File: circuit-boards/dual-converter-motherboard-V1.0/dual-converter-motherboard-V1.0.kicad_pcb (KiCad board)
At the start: 6 copper layers, 230 x 76 mm, 130 parts, among them J1 2601-1102, J2 2601-1102, J3 S4B-XH-SM4-TB, Q1 SUM110P08-11L-E3, Q2 DMP45H4D9HK3-13, Q3 SIHB068N60EF-GE3, U1 POWER_MANAGEMENT_MODULE, U2 HIGH-CURRENT_PHASE_MODULE_V1.0, U3 HIGH-VOLTAGE_PHASE_MODULE, U4 UCC23313BDWYR, U5 TMCS1133C1A, U6 UCC23313BDWYR, U7 UCC23313BDWYR, U8 SC0915

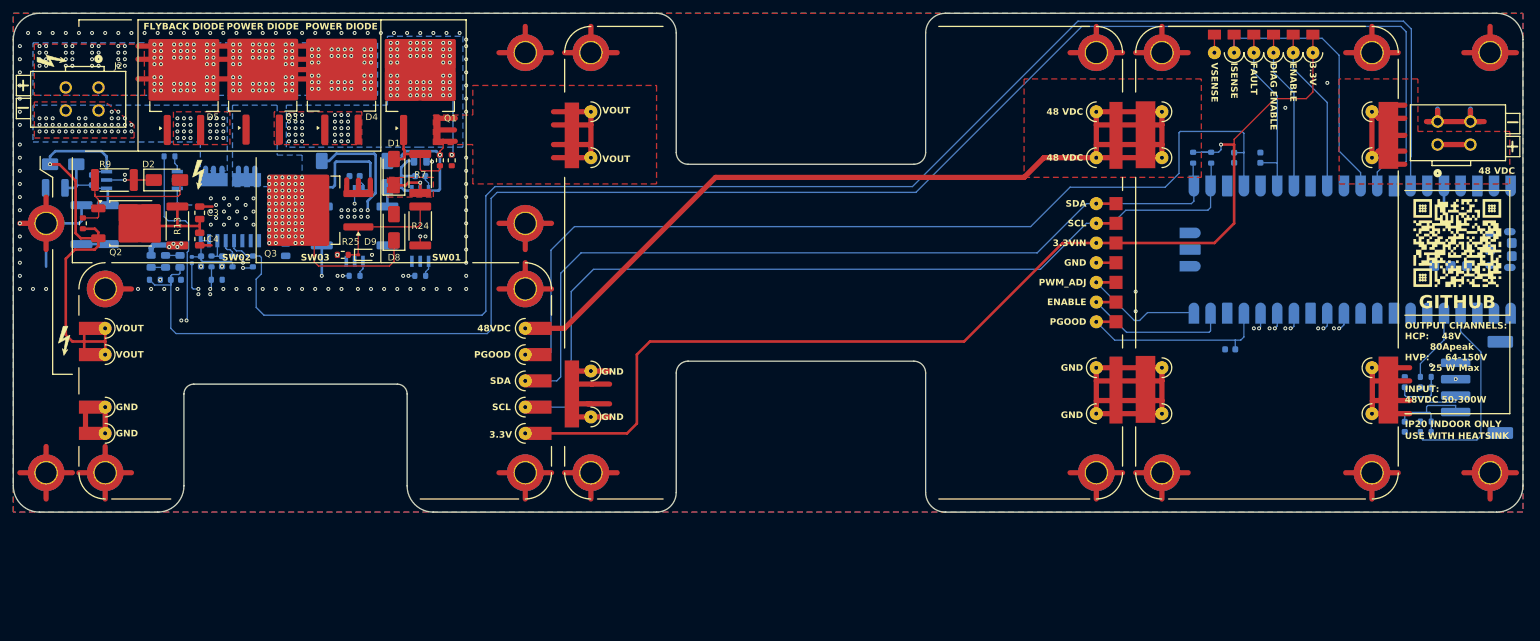
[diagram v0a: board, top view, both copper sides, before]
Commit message: begin replacing pogo pins with pin headers. todo: fix ugly schematic, add non power connections
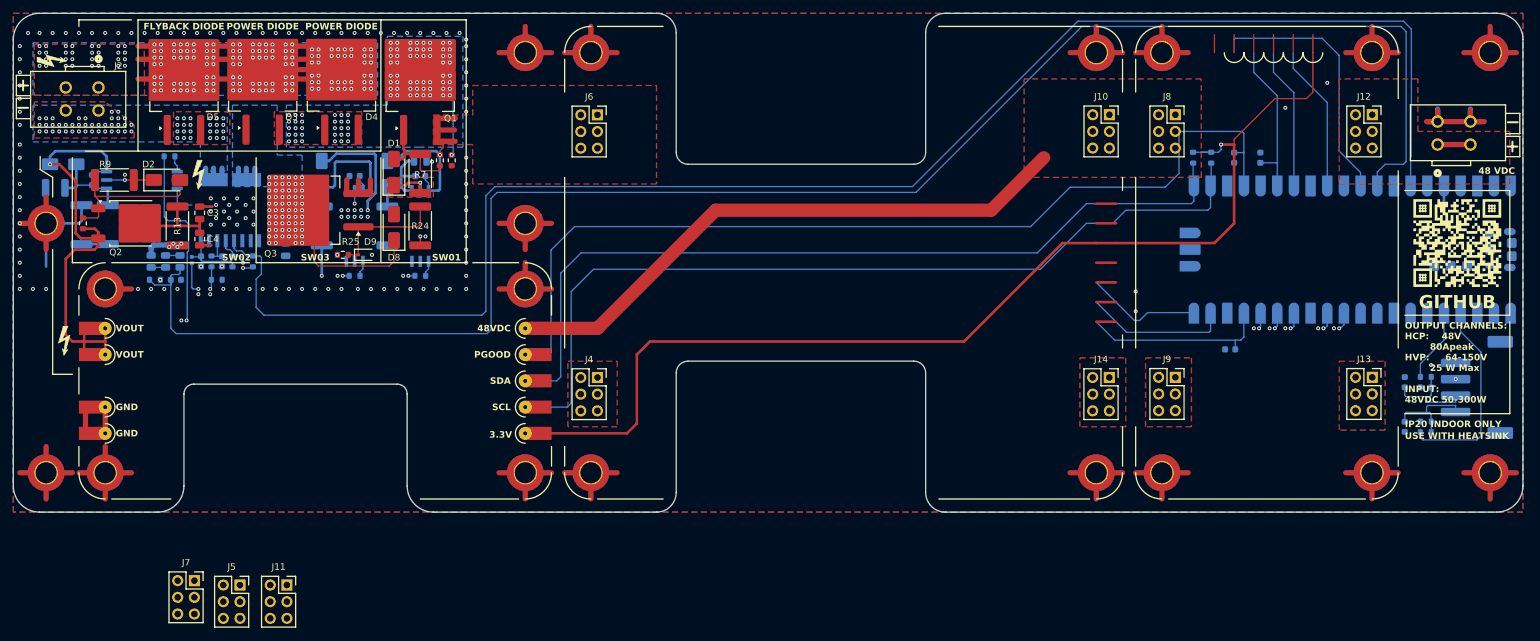
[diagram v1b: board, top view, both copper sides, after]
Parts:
- removed POGO10, POGO11, POGO12, POGO13, POGO14, POGO15, POGO16, POGO17, POGO18, POGO19, POGO20, POGO21, POGO27, POGO28, POGO29, POGO30: 0906-8-15-20-76-14-11-0, powercore-development:0906-8-15-20-76-14-11-0
- removed U1: POWER_MANAGEMENT_MODULE, powercore-development:POWER_MANAGEMENT_MODULE_FOOTPRINT_V1.0
- removed U2: HIGH-CURRENT_PHASE_MODULE_V1.0, powercore-development:HIGH-CURRENT_PHASE_MODULE_FOOTPRINT_V1.0
- added J10: Conn_02x03_Odd_Even, Connector_PinSocket_2.54mm:PinSocket_2x03_P2.54mm_Vertical, F.Cu at (189.0, 43.5)
- added J11: Conn_02x03_Odd_Even, Connector_PinSocket_2.54mm:PinSocket_2x03_P2.54mm_Vertical, F.Cu at (63.7, 115.1)
- added J12: Conn_02x03_Odd_Even, Connector_PinSocket_2.54mm:PinSocket_2x03_P2.54mm_Vertical, F.Cu at (229.0, 43.5)
- added J13: Conn_02x03_Odd_Even, Connector_PinSocket_2.54mm:PinSocket_2x03_P2.54mm_Vertical, F.Cu at (229.0, 83.5)
- added J14: Conn_02x03_Odd_Even, Connector_PinSocket_2.54mm:PinSocket_2x03_P2.54mm_Vertical, F.Cu at (189.0, 83.5)
- added J4: Conn_02x03_Odd_Even, Connector_PinSocket_2.54mm:PinSocket_2x03_P2.54mm_Vertical, F.Cu at (111.0, 83.5)
- added J5: Conn_02x03_Odd_Even, Connector_PinSocket_2.54mm:PinSocket_2x03_P2.54mm_Vertical, F.Cu at (56.5, 115.1)
- added J6: Conn_02x03_Odd_Even, Connector_PinSocket_2.54mm:PinSocket_2x03_P2.54mm_Vertical, F.Cu at (111.0, 43.5)
- added J7: Conn_02x03_Odd_Even, Connector_PinSocket_2.54mm:PinSocket_2x03_P2.54mm_Vertical, F.Cu at (49.6, 114.4)
- added J8: Conn_02x03_Odd_Even, Connector_PinSocket_2.54mm:PinSocket_2x03_P2.54mm_Vertical, F.Cu at (199.0, 43.5)
- added J9: Conn_02x03_Odd_Even, Connector_PinSocket_2.54mm:PinSocket_2x03_P2.54mm_Vertical, F.Cu at (199.0, 83.5)
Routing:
- net GND: track 418.5 -> 306.5 mm
- net +48V: track 195.1 -> 133.1 mm
- net /BUCK-CONVERTER-OUTPUT: track 57.5 -> 28.9 mm
- net /48VIN: track 27.7 -> 5.00 mm
- net /PMM_VSENSE: track 2.75 -> 0.00 mm
- net (no net): track 0.00 -> 2.75 mm

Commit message: add signal connector sockets, fix routing, rough-out locations
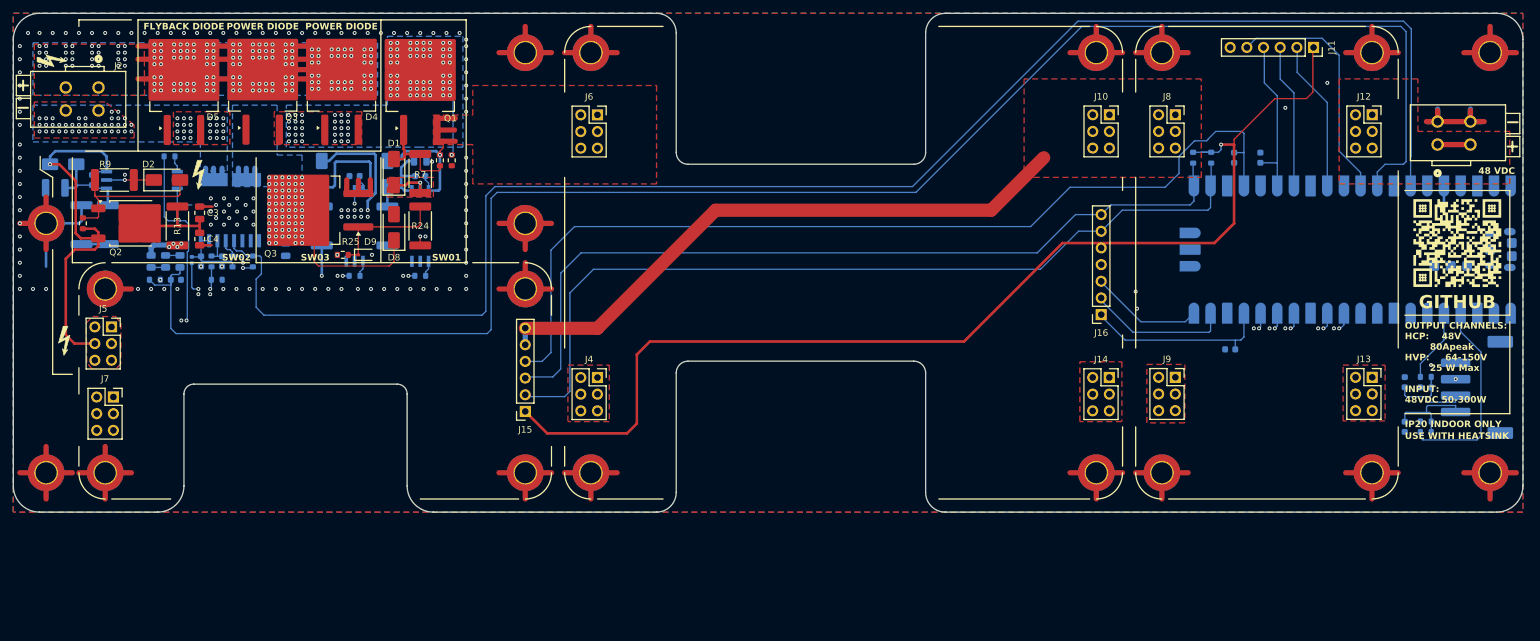
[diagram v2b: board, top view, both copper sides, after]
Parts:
- removed POGO1, POGO2, POGO22, POGO23, POGO24, POGO25, POGO26, POGO3, POGO4, POGO5, POGO6, POGO7, POGO8, POGO9: 0906-8-15-20-76-14-11-0, powercore-development:0906-8-15-20-76-14-11-0
- removed U3: HIGH-VOLTAGE_PHASE_MODULE, powercore-development:HIGH-VOLTAGE_PHASE_MODULE_FOOTPRINT_V1.0
- added J15: Conn_01x06_Socket, Connector_PinSocket_2.54mm:PinSocket_1x06_P2.54mm_Vertical, F.Cu at (100.0, 88.7)
- added J16: Conn_01x07_Socket, Connector_PinSocket_2.54mm:PinSocket_1x07_P2.54mm_Vertical, F.Cu at (187.8, 73.9)
- J11: value Conn_02x03_Odd_Even -> Conn_01x06_Socket; footprint Connector_PinSocket_2.54mm:PinSocket_2x03_P2.54mm_Vertical -> Connector_PinSocket_2.54mm:PinSocket_1x06_P2.54mm_Vertical
- moved J11 176.6 mm to (220.1, 33.2), turned to -90 degrees
- moved J5 43.9 mm to (37.0, 75.8)
- moved J7 30.6 mm to (37.2, 86.5)
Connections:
- J11 pad 1: +48V -> +3.3V
- J11 pad 2: +48V -> /PMM_ENABLE
- J11 pad 3: +48V -> /PMM_DIAG_EN
- J11 pad 4: +48V -> /PMM_FAULT
- J11 pad 5: +48V -> /PMM_ISENSE
- J11 pad 6: +48V -> /PMM_VSENSE
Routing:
- net GND: track 306.5 -> 289.5 mm
- net /BOOST-CONVERTER-OUTPUT: track 74.8 -> 58.9 mm
- net /I2C_SCL: track 139.8 -> 132.1 mm
- net /I2C_SDA: track 134.3 -> 127.4 mm
- net /PMM_ISENSE: track 43.2 -> 37.0 mm
- net /BOOST_PGOOD: track 149.0 -> 144.3 mm
- net /BUCK_ENABLE: track 25.1 -> 21.8 mm
- net /BUCK_POWER_GOOD: track 31.9 -> 28.7 mm
- net (no net): track 2.75 -> 0.00 mm
- net /BUCK_ADJ_PWM: track 20.8 -> 18.1 mm
- net /PMM_FAULT: track 27.1 -> 24.6 mm
- net +48V: track 133.1 -> 135.6 mm
- net /PMM_DIAG_EN: track 24.3 -> 22.0 mm
- net /PMM_ENABLE: track 25.2 -> 23.0 mm
- added copper zone on F.Cu, net /BOOST-CONVERTER-OUTPUT

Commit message: motherboard: align and lock connectors and mountpoints, add cutout for pico test points, fix pico footprint, improve tracks
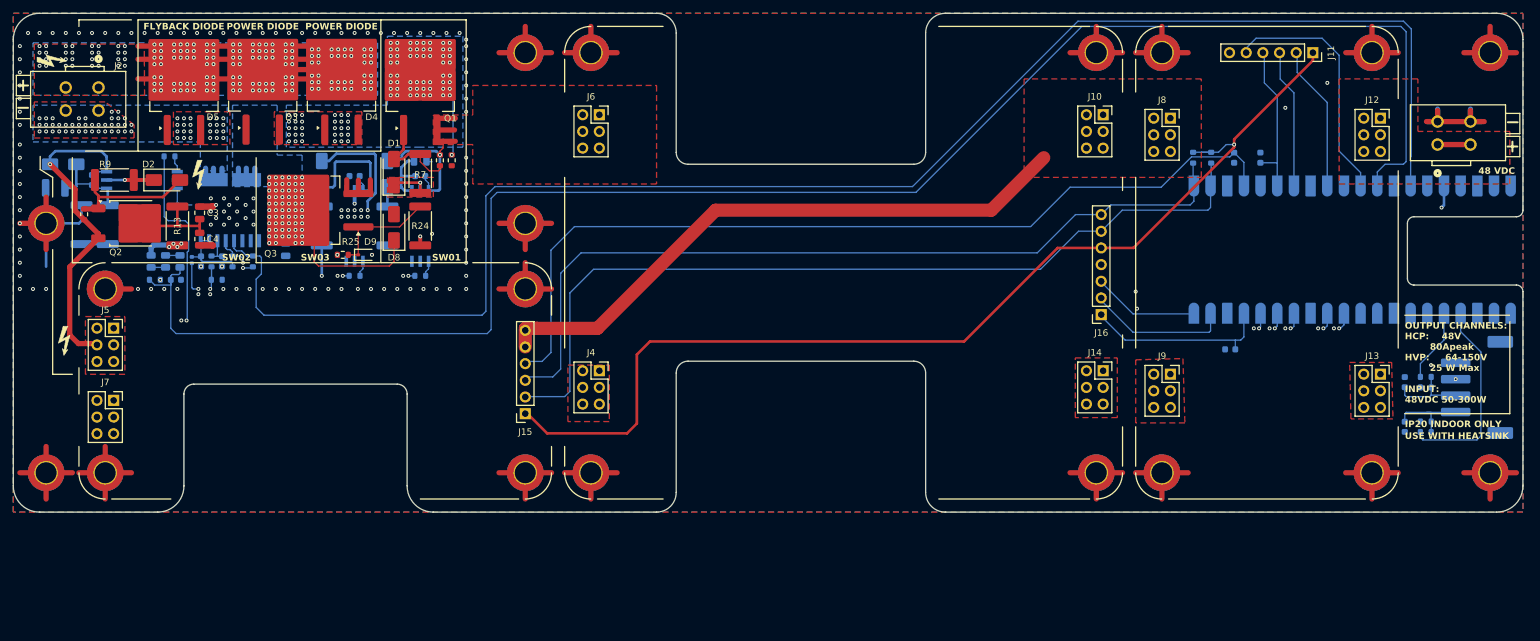
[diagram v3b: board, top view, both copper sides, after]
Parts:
- removed G***: LOGO, powercore-development:powercoreV3github
- moved J14 1.40 mm to (188.0, 82.5)
- moved R6 1.39 mm to (32.8, 58.6)
- moved J12 1.35 mm to (230.3, 44.0)
- moved J13 1.34 mm to (230.3, 83.0)
- moved J4 1.07 mm to (111.3, 82.5)
- moved J10 0.96 mm to (188.0, 43.5)
- moved J8 0.91 mm to (198.3, 44.0)
- moved J9 0.89 mm to (198.3, 83.0)
- moved J11 0.81 mm to (220.0, 34.0)
- moved J7 0.52 mm to (37.3, 87.0)
- moved J5 0.38 mm to (37.3, 76.0)
- moved J15 0.34 mm to (100.0, 89.0)
- moved J6 0.29 mm to (111.3, 43.5)
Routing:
- net +3.3V: track 355.6 -> 346.2 mm
- net /BOOST-CONVERTER-OUTPUT: track 58.9 -> 50.4 mm
- net /BOOST_PGOOD: track 144.3 -> 136.0 mm
- net +48V: track 135.6 -> 139.9 mm
- net Net-(J3-Pin_3): track 14.4 -> 12.4 mm
- net Net-(J3-Pin_4): track 14.6 -> 12.8 mm
- net Net-(D9-K): track 18.1 -> 16.5 mm
- net Net-(D2-A): track 23.6 -> 22.0 mm
- net /BUCK_ADJ_PWM: track 18.1 -> 17.1 mm
- net GND: track 289.5 -> 290.1 mm, vias 147 -> 145
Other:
- outline, holes or cut-outs redrawn
- board text added: "cut out here"
